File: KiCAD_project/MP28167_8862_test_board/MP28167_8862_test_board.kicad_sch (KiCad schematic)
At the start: 34 parts, among them IC1 MP8862GQ-0000-Z, J1 Conn_01x04_Male, J2 Conn_01x02_Female, J3 Conn_01x02_Female, J4 Conn_01x02_Female, J5 Conn_01x02_Female, U1 AP63203WU

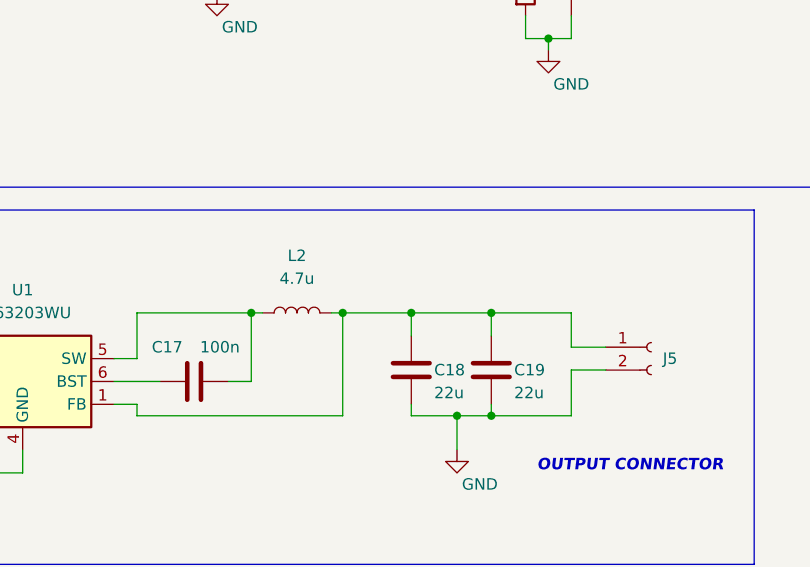
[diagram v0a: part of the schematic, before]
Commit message: schematic update
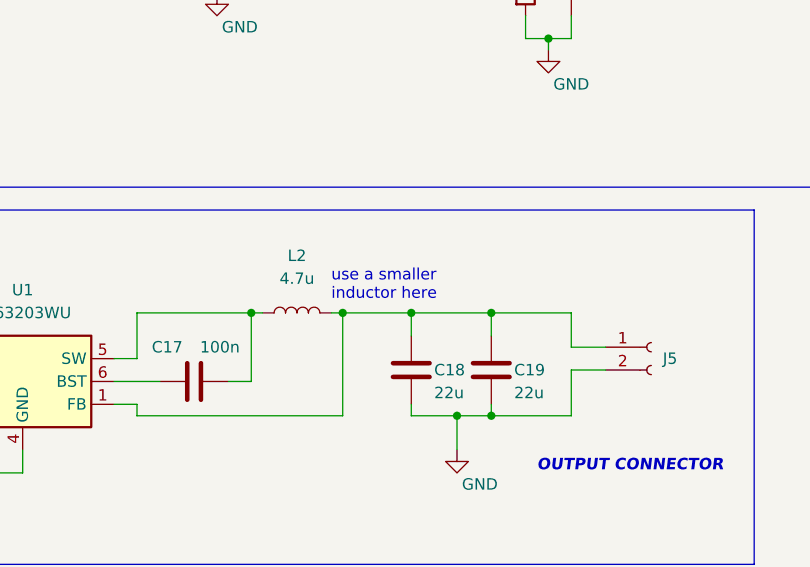
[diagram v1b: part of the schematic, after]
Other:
- note added: "use a smaller inductor here"
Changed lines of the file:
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@@
     (effects (font (size 1.27 1.27) (thickness 0.254) bold italic) (justify left bottom))
+  )
+  (text "use a smaller \ninductor here" (at 102.87 124.46 0)
+    (effects (font (size 1.27 1.27)) (justify left bottom))
   )
   (text "INPUT CONNECTOR\n" (at 22.86 66.04 0)

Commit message: first schematic
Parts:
- added C20, C34: 100u, symbol Device:C_Polarized
- added C21, C29, C30, C31, C32, C33: 22u, symbol Device:C
- added C22, C24, C26, C28: 100n, symbol Device:C
- added C23, C25: 22n, symbol Device:C
- added C27: 1u, symbol Device:C
- added J6, J7: Conn_01x02_Female, symbol Connector:Conn_01x02_Female
- added J8: Conn_01x04_Male, symbol Connector:Conn_01x04_Male
- added L3: 4.7u, symbol Device:L
- added R10, R8: 0, symbol Device:R
- added R11: 787k, symbol Device:R
- added R12: 430k, symbol Device:R
- added R13: 53.6k, symbol Device:R
- added R7: 499k, symbol Device:R
- added R9: 21.5k, symbol Device:R
- added U2: MP28167GQ-A-Z, QFN-16_MP28167_MNP, symbol 2023-03-10_09-43-26:MP28167GQ-A-Z
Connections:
- net GND: now also C20.2, C21.2, C22.2, C23.2, C25.2, C27.2, C28.2, C29.2, C30.2, C31.2, C32.2, C33.2, C34.2, J6.1 (Pin_1), J7.2 (Pin_2), J8.4 (Pin_4), R13.2, R9.2, U2.10 (AGND), U2.11 (GND), U2.2 (GND)
- new net: C24.2, R8.1
- new net: R8.2, U2.16 (BST1)
- new net: C20.1, C21.1, C22.1, J6.2 (Pin_2), R7.1, U2.1 (IN)
- new net: C28.1, C29.1, C30.1, C31.1, C32.1, C33.1, C34.1, J7.1 (Pin_1), R12.1, U2.12 (OUT)
- new net: C26.2, R10.1
- new net: R10.2, U2.13 (BST2)
- new net: C23.1, R7.2, U2.3 (EN)
- new net: C26.1, L3.2, U2.14 (SW2)
- new net: C24.1, L3.1, U2.15 (SW1)
- new net: C25.1, R9.1, U2.7 (OC)
- new net: R11.1, U2.8 (FB)
- new net: C27.1, U2.9 (VCC)
- new net: R11.2, R12.2, R13.1
- new net ALT_28167: J8.1 (Pin_1), U2.4 (ALT)
- new net SCL_28167: J8.2 (Pin_2), U2.5 (SCL)
- new net SDA_28167: J8.3 (Pin_3), U2.6 (SDA)
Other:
- note added: "MP28167"
- title: (none) -> PM8862 / PM28167 dev board

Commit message: footprint update
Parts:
- U2: footprint QFN-16_MP28167_MNP -> footprints:MP28167GQ-A-Z
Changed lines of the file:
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@@
       (effects (font (size 1.524 1.524)))
     )
-    (property "Footprint" "QFN-16_MP28167_MNP" (id 2) (at 127 190.754 0)
+    (property "Footprint" "footprints:MP28167GQ-A-Z" (id 2) (at 127 190.754 0)
       (effects (font (size 1.524 1.524)) hide)
     )
@@
     )
     (path "/82d40548-c1ae-451b-bea2-e6eb9c8d37b8"
-      (reference "U2") (unit 1) (value "MP28167GQ-A-Z") (footprint "QFN-16_MP28167_MNP")
-    )
-  )
+      (reference "U2") (unit 1) (value "MP28167GQ-A-Z") (footprint "footprints:MP28167GQ-A-Z")
+    )
+  )

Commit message: pcb layout update
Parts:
- C1, C15, C20, C34: footprint (none) -> Capacitor_SMD:CP_Elec_5x5.3
- C10, C11, C12, C13, C14, C16, C17, C18, C19, C21, C24, C26, C29, C3, C30, C31, C32, C33, C5, C7, C9: footprint (none) -> Capacitor_SMD:C_0805_2012Metric_Pad1.18x1.45mm_HandSolder
- C2, C22, C23, C25, C27, C28, C4, C6, C8: footprint (none) -> Capacitor_SMD:C_0603_1608Metric_Pad1.08x0.95mm_HandSolder
- J1, J8: footprint (none) -> Connector_PinHeader_2.54mm:PinHeader_1x04_P2.54mm_Vertical
- J2, J3, J4, J5, J6, J7: footprint (none) -> Connector_Wire:SolderWire-0.1sqmm_1x02_P3.6mm_D0.4mm_OD1mm
- L1, L3: footprint (none) -> footprints:EXL1V0705 inductor
- L2: footprint (none) -> footprints:SDES064T-4R7MS inductor
- R1, R10, R11, R12, R13, R2, R3, R4, R5, R6, R7, R8, R9: footprint (none) -> Resistor_SMD:R_0603_1608Metric_Pad0.98x0.95mm_HandSolder
